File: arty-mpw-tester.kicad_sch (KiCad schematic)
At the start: 107 parts, among them J10 61300211121, J11 61300211121, J12 61300211121, J14 61300311121, J15 61300311121, J18 61300411121, J19 61300711121, J20 61300411121, J3 arty_chipKIT_connector, J4 61300211121, J5 61300311121, J6 61300211121, J7 61300211121, J8 61300211121, J9 61300211121, Q1 DTC014TEBTL, SW1 JS202011JCQN, SW3 JS202011JCQN, U1 PAC1954T-E/4MX, U3 PAC1954T-E/4MX, U4 MAX811REUS+T, U5 NTS0102DP, U6 MCP4661-103E/ML, U7 Caravel_breakout_PCB_flexypin, U8 W25Q32FVSS, U9 MIC2211-AAYML-TR, Y2 ECS-2520MVLC-100-BN-TR

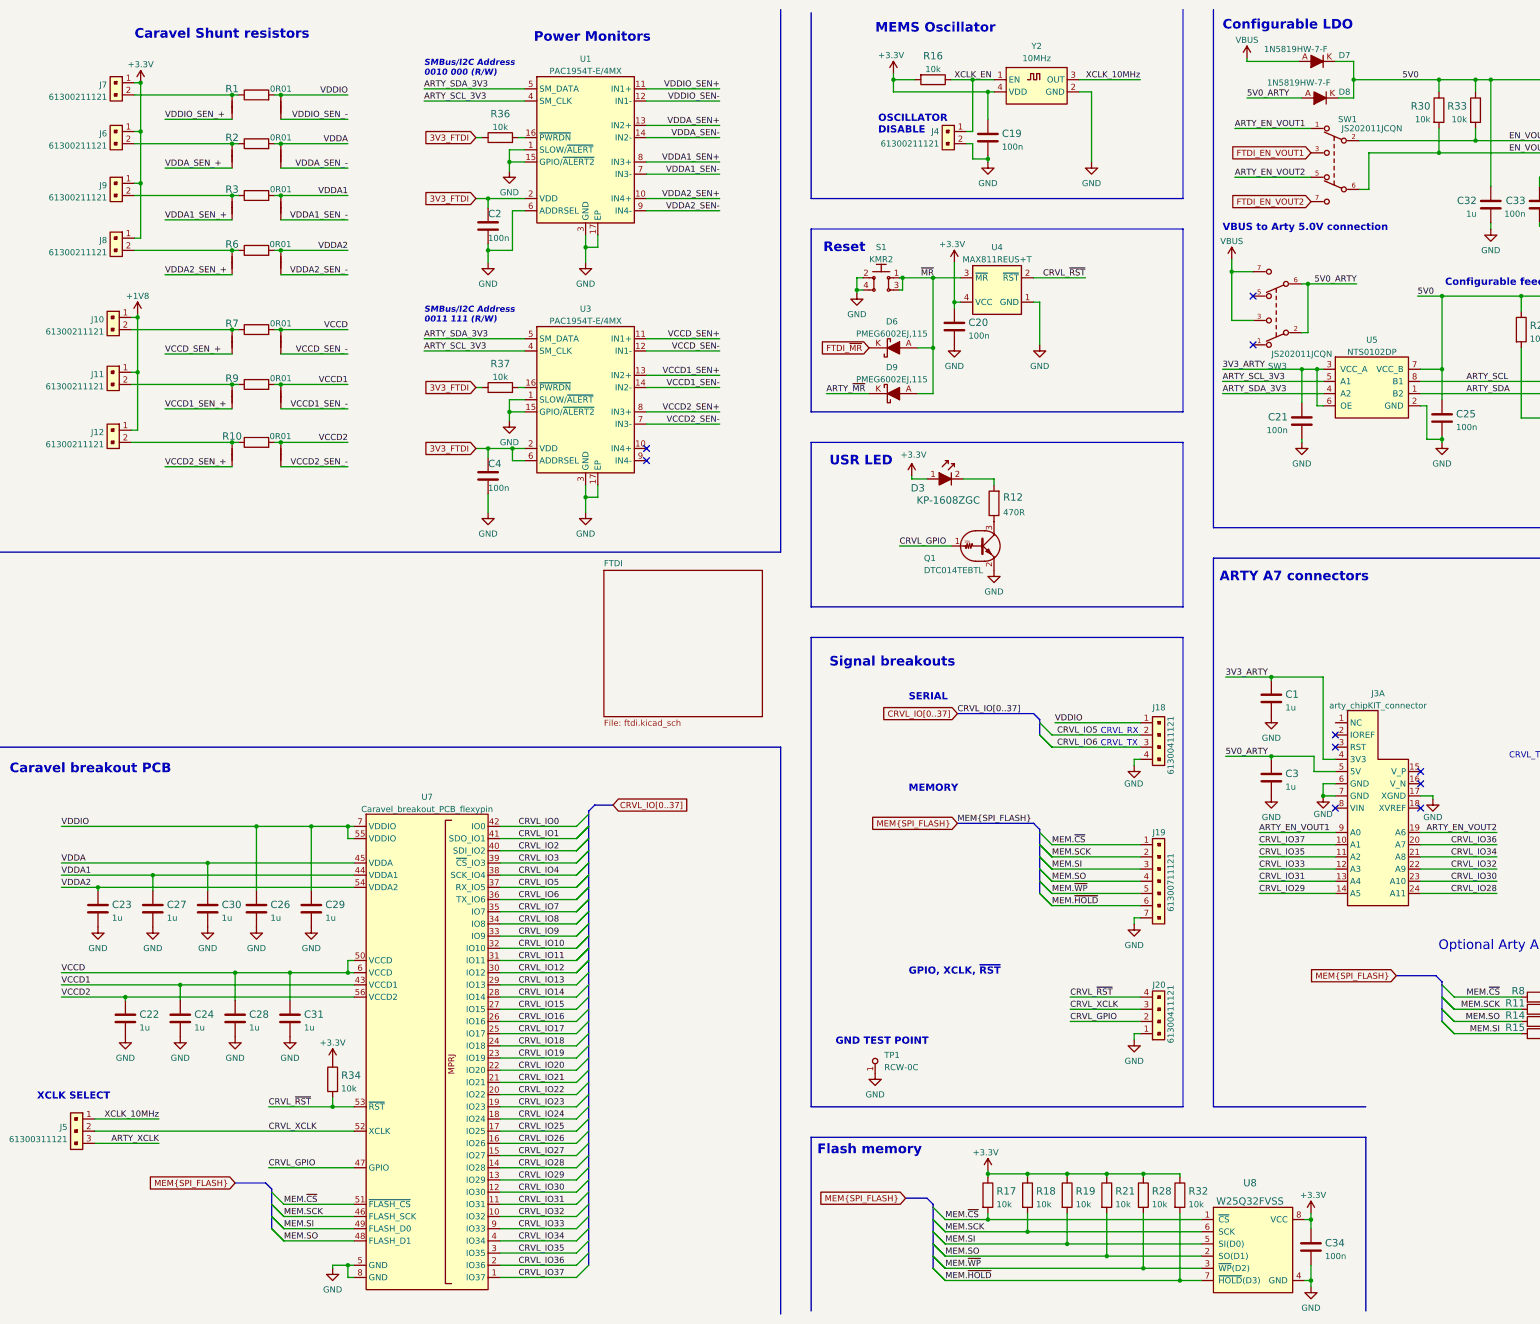
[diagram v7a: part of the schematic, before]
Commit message: Imported all changes to PCB. Cleared old tracks. Started placement and layout
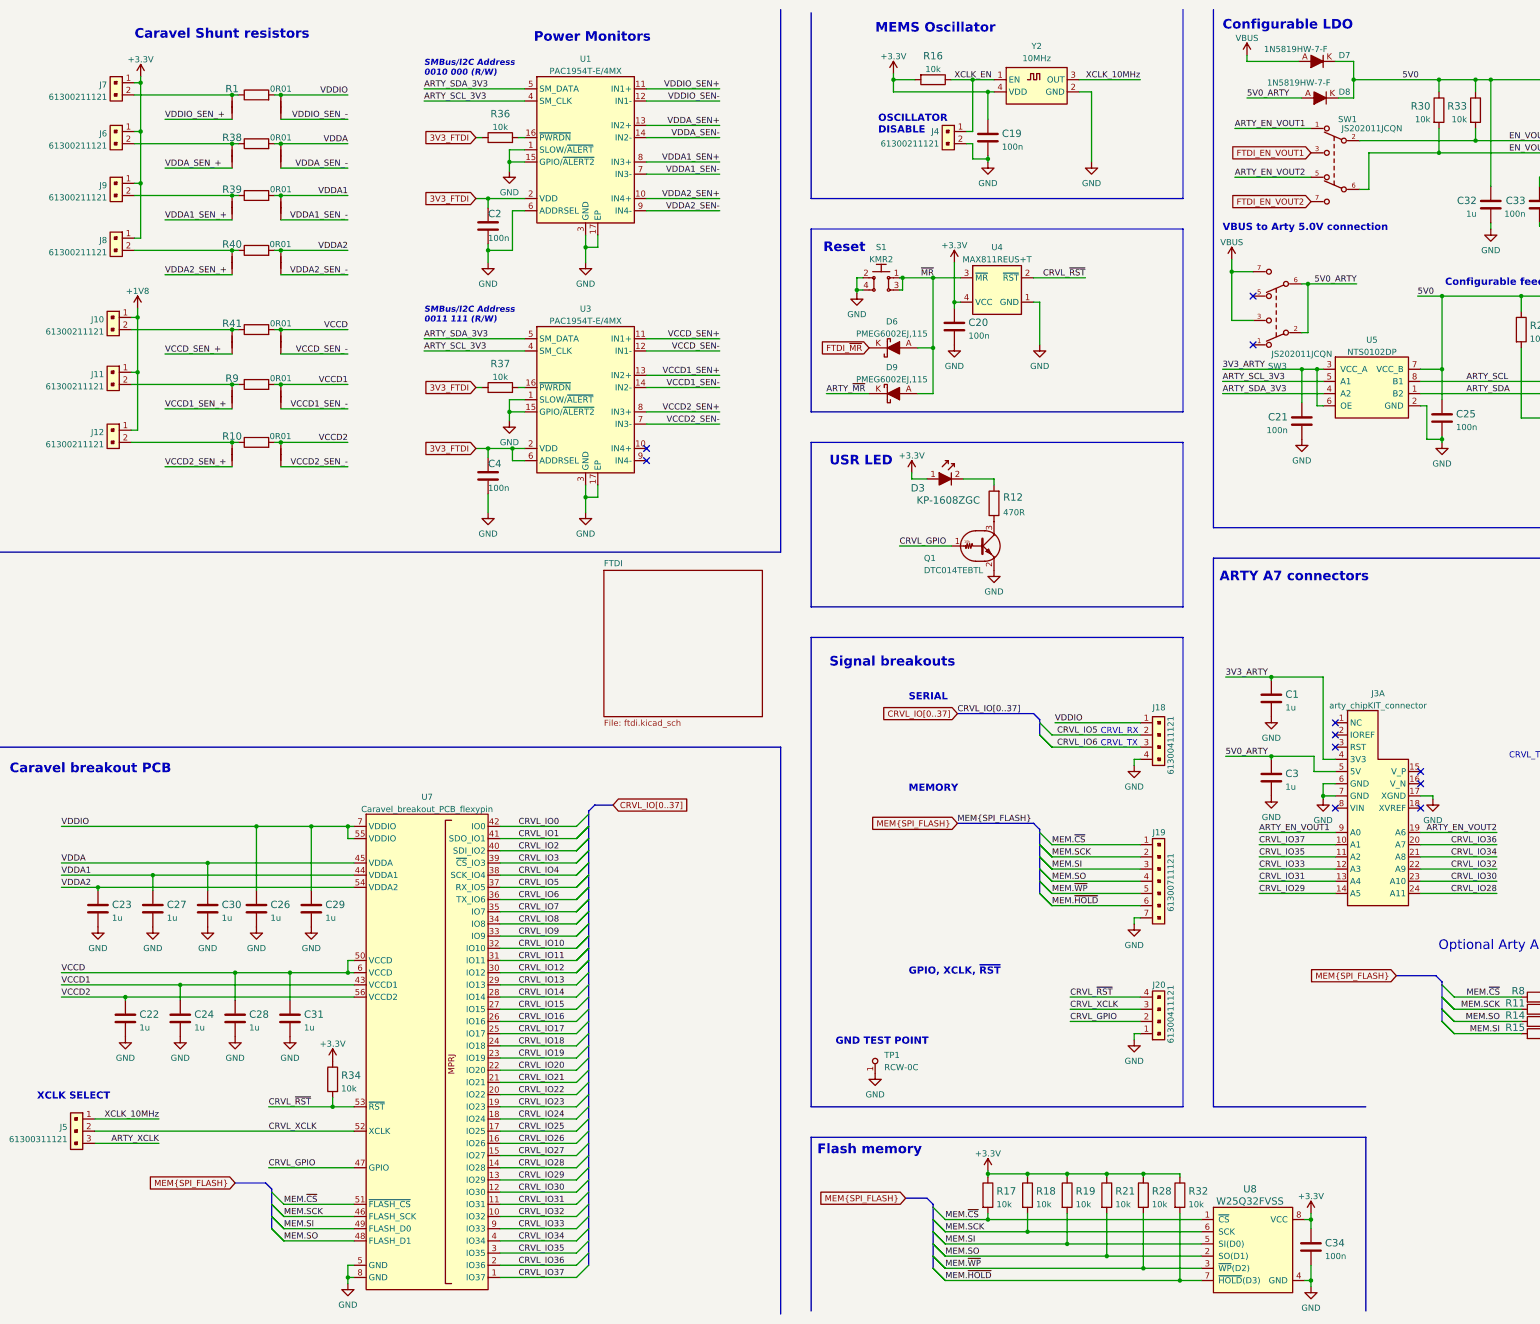
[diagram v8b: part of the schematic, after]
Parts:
- renumbered R2 to R38, R3 to R39, R6 to R40, R7 to R41
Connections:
- no-connect marks 12 -> 13
